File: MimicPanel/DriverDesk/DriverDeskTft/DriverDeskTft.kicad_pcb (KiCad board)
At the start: 4 copper layers, 84.5 x 92 mm, 25 parts, among them SW1 SW_Push, SW10 SW_Push, SW2 SW_Push, SW3 SW_Push, SW4 SW_Push, SW5 SW_Push, SW6 SW_Push, SW7 SW_Push, SW8 SW_Push, SW9 SW_Push

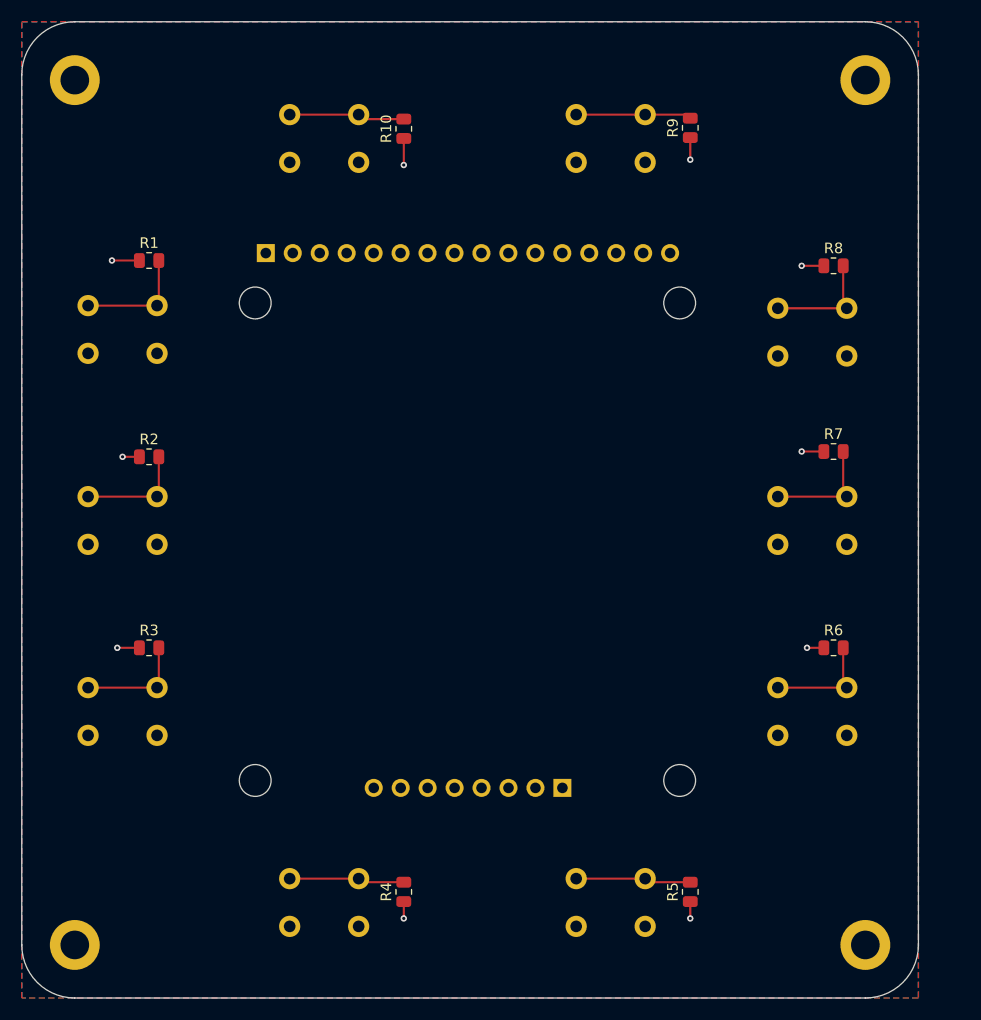
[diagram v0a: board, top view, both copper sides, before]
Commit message: updated positions
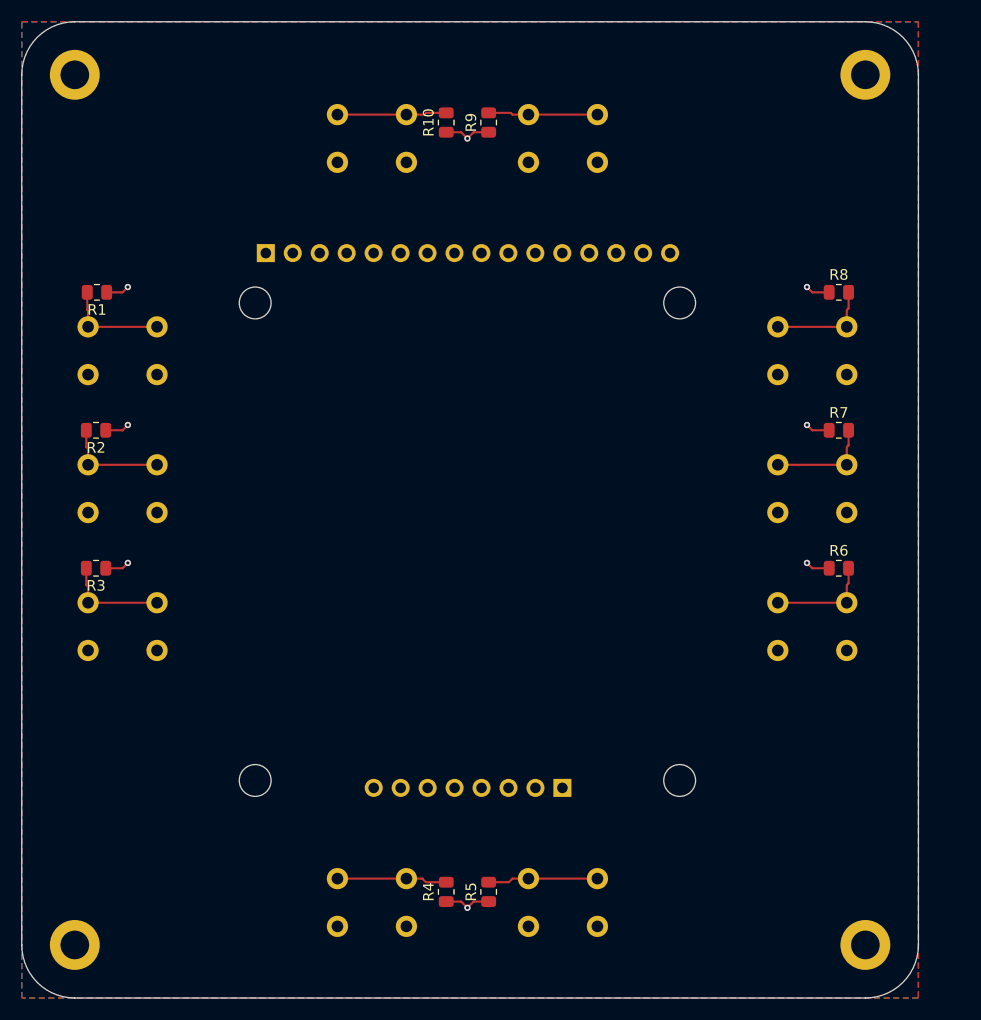
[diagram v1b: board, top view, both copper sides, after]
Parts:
- moved R9 19.0 mm to (102.0, 62.5)
- moved R5 19.0 mm to (102.0, 135.0)
- moved R3 9.01 mm to (65.0, 104.5), turned to 180 degrees
- moved SW3 8.00 mm to (70.8, 107.8)
- moved SW6 8.00 mm to (135.8, 107.8)
- moved R6 7.52 mm to (135.0, 104.5)
- moved R1 5.76 mm to (65.1, 78.5), turned to 180 degrees
- moved R2 5.59 mm to (65.0, 91.5), turned to 180 degrees
- moved SW10 4.50 mm to (94.2, 61.8)
- moved SW4 4.50 mm to (94.2, 133.8)
- moved SW5 4.50 mm to (112.2, 133.8)
- moved SW9 4.50 mm to (112.2, 61.8)
- moved R10 4.04 mm to (98.0, 62.5)
- moved R4 4.00 mm to (98.0, 135.0)
- moved SW2 3.00 mm to (70.8, 94.8)
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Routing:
- net VCC: track 19.8 -> 22.7 mm, vias 10 -> 8
- net /Btn/btn_7: track 10.9 -> 9.82 mm
- net /Btn/btn_1: track 10.8 -> 9.78 mm
- net /Btn/btn_6: track 10.6 -> 9.82 mm
- net /Btn/btn_4: track 10.9 -> 10.3 mm
- net /Btn/btn_8: track 10.4 -> 9.82 mm
- net /Btn/btn_5: track 10.9 -> 10.3 mm
- net /Btn/btn_9: track 10.9 -> 10.4 mm
- net /Btn/btn_3: track 10.3 -> 9.82 mm
- net /Btn/btn_2: track 10.3 -> 9.82 mm
- net /Btn/btn_10: track 10.9 -> 10.4 mm

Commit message: TftModule
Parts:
- SW1, SW10, SW2, SW3, SW4, SW5, SW6, SW7, SW8, SW9: footprint Button_Switch_THT:SW_PUSH_6mm -> Button_Switch_THT:SW_PUSH_6mm_H5mm
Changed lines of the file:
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@@
 		(tags "resistor")
 		(property "Reference" "R2"
-			(at 0 -1.65 360)
+			(at 0 -1.65 0)
 			(layer "F.SilkS")
 			(effects
@@
 		)
 		(property "Value" "R"
-			(at 0 1.65 360)
+			(at 0 1.65 0)
 			(layer "F.Fab")
 			(effects
@@
 		)
 		(fp_text user "${REFERENCE}"
-			(at 0 0 360)
+			(at 0 0 0)
 			(layer "F.Fab")
 			(effects
@@
 		(tags "resistor")
 		(property "Reference" "R3"
-			(at 0 -1.65 360)
+			(at 0 -1.65 0)
 			(layer "F.SilkS")
 			(effects
@@
 		)
 		(property "Value" "R"
-			(at 0 1.65 360)
+			(at 0 1.65 0)
 			(layer "F.Fab")
 			(effects
@@
 		)
 		(fp_text user "${REFERENCE}"
-			(at 0 0 360)
+			(at 0 0 0)
 			(layer "F.Fab")
 			(effects
@@
 		(tags "resistor")
 		(property "Reference" "R1"
-			(at 0 -1.65 360)
+			(at 0 -1.65 0)
 			(layer "F.SilkS")
 			(effects
@@
 		)
 		(property "Value" "R"
-			(at 0 1.65 360)
+			(at 0 1.65 0)
 			(layer "F.Fab")
 			(effects
@@
 		)
 		(fp_text user "${REFERENCE}"
-			(at 0 0 360)
+			(at 0 0 0)
 			(layer "F.Fab")
 			(effects
@@
 		)
 	)
-	(footprint "Button_Switch_THT:SW_PUSH_6mm"
+	(footprint "Button_Switch_THT:SW_PUSH_6mm_H5mm"
 		(layer "B.Cu")
 		(at 94.25 61.75 180)
-		(descr "Generic 6mm SW tactile push button")
+		(descr "tactile push button, 6x6mm e.g. PHAP33xx series, height=5mm")
 		(tags "tact sw push 6mm")
 		(property "Reference" "SW10"
@@
 			)
 		)
-		(property "Footprint" "Button_Switch_THT:SW_PUSH_6mm"
+		(property "Footprint" "Button_Switch_THT:SW_PUSH_6mm_H5mm"
 			(at 0 0 0)
 			(unlocked yes)
@@
 			(pintype "passive")
 		)
-		(model "${KICAD8_3DMODEL_DIR}/Button_Switch_THT.3dshapes/SW_PUSH_6mm.wrl"
+		(model "${KICAD8_3DMODEL_DIR}/Button_Switch_THT.3dshapes/SW_PUSH_6mm_H5mm.wrl"
 			(offset
 				(xyz 0 0 0)
@@
 		)
 	)
-	(footprint "Button_Switch_THT:SW_PUSH_6mm"
+	(footprint "Button_Switch_THT:SW_PUSH_6mm_H5mm"
 		(layer "B.Cu")
 		(at 94.25 133.75 180)
-		(descr "Generic 6mm SW tactile push button")
+		(descr "tactile push button, 6x6mm e.g. PHAP33xx series, height=5mm")
 		(tags "tact sw push 6mm")
 		(property "Reference" "SW4"
@@
 			)
 		)
-		(property "Footprint" "Button_Switch_THT:SW_PUSH_6mm"
+		(property "Footprint" "Button_Switch_THT:SW_PUSH_6mm_H5mm"
 			(at 0 0 0)
 			(unlocked yes)
@@
 			(pintype "passive")
 		)
-		(model "${KICAD8_3DMODEL_DIR}/Button_Switch_THT.3dshapes/SW_PUSH_6mm.wrl"
+		(model "${KICAD8_3DMODEL_DIR}/Button_Switch_THT.3dshapes/SW_PUSH_6mm_H5mm.wrl"
 			(offset
 				(xyz 0 0 0)
@@
 		)
 	)
-	(footprint "Button_Switch_THT:SW_PUSH_6mm"
+	(footprint "Button_Switch_THT:SW_PUSH_6mm_H5mm"
 		(layer "B.Cu")
 		(at 135.75 81.75 180)
-		(descr "Generic 6mm SW tactile push button")
+		(descr "tactile push button, 6x6mm e.g. PHAP33xx series, height=5mm")
 		(tags "tact sw push 6mm")
 		(property "Reference" "SW8"
@@
 			)
 		)
-		(property "Footprint" "Button_Switch_THT:SW_PUSH_6mm"
+		(property "Footprint" "Button_Switch_THT:SW_PUSH_6mm_H5mm"
 			(at 0 0 0)
 			(unlocked yes)
@@
 			(pintype "passive")
 		)
-		(model "${KICAD8_3DMODEL_DIR}/Button_Switch_THT.3dshapes/SW_PUSH_6mm.wrl"
+		(model "${KICAD8_3DMODEL_DIR}/Button_Switch_THT.3dshapes/SW_PUSH_6mm_H5mm.wrl"
 			(offset
 				(xyz 0 0 0)
@@
 		)
 	)
-	(footprint "Button_Switch_THT:SW_PUSH_6mm"
+	(footprint "Button_Switch_THT:SW_PUSH_6mm_H5mm"
 		(layer "B.Cu")
 		(at 70.75 94.75 180)
-		(descr "Generic 6mm SW tactile push button")
+		(descr "tactile push button, 6x6mm e.g. PHAP33xx series, height=5mm")
 		(tags "tact sw push 6mm")
 		(property "Reference" "SW2"
@@
 			)
 		)
-		(property "Footprint" "Button_Switch_THT:SW_PUSH_6mm"
+		(property "Footprint" "Button_Switch_THT:SW_PUSH_6mm_H5mm"
 			(at 0 0 0)
 			(unlocked yes)
@@
 			(pintype "passive")
 		)
-		(model "${KICAD8_3DMODEL_DIR}/Button_Switch_THT.3dshapes/SW_PUSH_6mm.wrl"
+		(model "${KICAD8_3DMODEL_DIR}/Button_Switch_THT.3dshapes/SW_PUSH_6mm_H5mm.wrl"
 			(offset
 				(xyz 0 0 0)
@@
 		)
 	)
-	(footprint "Button_Switch_THT:SW_PUSH_6mm"
+	(footprint "Button_Switch_THT:SW_PUSH_6mm_H5mm"
 		(layer "B.Cu")
 		(at 112.25 133.75 180)
-		(descr "Generic 6mm SW tactile push button")
+		(descr "tactile push button, 6x6mm e.g. PHAP33xx series, height=5mm")
 		(tags "tact sw push 6mm")
 		(property "Reference" "SW5"
@@
 			)
 		)
-		(property "Footprint" "Button_Switch_THT:SW_PUSH_6mm"
+		(property "Footprint" "Button_Switch_THT:SW_PUSH_6mm_H5mm"
 			(at 0 0 0)
 			(unlocked yes)
@@
 			(pintype "passive")
 		)
-		(model "${KICAD8_3DMODEL_DIR}/Button_Switch_THT.3dshapes/SW_PUSH_6mm.wrl"
+		(model "${KICAD8_3DMODEL_DIR}/Button_Switch_THT.3dshapes/SW_PUSH_6mm_H5mm.wrl"
 			(offset
 				(xyz 0 0 0)
@@
 		)
 	)
-	(footprint "Button_Switch_THT:SW_PUSH_6mm"
+	(footprint "Button_Switch_THT:SW_PUSH_6mm_H5mm"
 		(layer "B.Cu")
 		(at 135.75 94.75 180)
-		(descr "Generic 6mm SW tactile push button")
+		(descr "tactile push button, 6x6mm e.g. PHAP33xx series, height=5mm")
 		(tags "tact sw push 6mm")
 		(property "Reference" "SW7"
@@
 			)
 		)
-		(property "Footprint" "Button_Switch_THT:SW_PUSH_6mm"
+		(property "Footprint" "Button_Switch_THT:SW_PUSH_6mm_H5mm"
 			(at 0 0 0)
 			(unlocked yes)
@@
 			(pintype "passive")
 		)
-		(model "${KICAD8_3DMODEL_DIR}/Button_Switch_THT.3dshapes/SW_PUSH_6mm.wrl"
+		(model "${KICAD8_3DMODEL_DIR}/Button_Switch_THT.3dshapes/SW_PUSH_6mm_H5mm.wrl"
 			(offset
 				(xyz 0 0 0)
@@
 		)
 	)
-	(footprint "Button_Switch_THT:SW_PUSH_6mm"
+	(footprint "Button_Switch_THT:SW_PUSH_6mm_H5mm"
 		(layer "B.Cu")
 		(at 70.75 81.75 180)
-		(descr "Generic 6mm SW tactile push button")
+		(descr "tactile push button, 6x6mm e.g. PHAP33xx series, height=5mm")
 		(tags "tact sw push 6mm")
 		(property "Reference" "SW1"
@@
 			)
 		)
-		(property "Footprint" "Button_Switch_THT:SW_PUSH_6mm"
+		(property "Footprint" "Button_Switch_THT:SW_PUSH_6mm_H5mm"
 			(at 0 0 0)
 			(unlocked yes)
@@
 			(pintype "passive")
 		)
-		(model "${KICAD8_3DMODEL_DIR}/Button_Switch_THT.3dshapes/SW_PUSH_6mm.wrl"
+		(model "${KICAD8_3DMODEL_DIR}/Button_Switch_THT.3dshapes/SW_PUSH_6mm_H5mm.wrl"
 			(offset
 				(xyz 0 0 0)
@@
 		)
 	)
-	(footprint "Button_Switch_THT:SW_PUSH_6mm"
+	(footprint "Button_Switch_THT:SW_PUSH_6mm_H5mm"
 		(layer "B.Cu")
 		(at 70.75 107.75 180)
-		(descr "Generic 6mm SW tactile push button")
+		(descr "tactile push button, 6x6mm e.g. PHAP33xx series, height=5mm")
 		(tags "tact sw push 6mm")
 		(property "Reference" "SW3"
@@
 			)
 		)
-		(property "Footprint" "Button_Switch_THT:SW_PUSH_6mm"
+		(property "Footprint" "Button_Switch_THT:SW_PUSH_6mm_H5mm"
 			(at 0 0 0)
 			(unlocked yes)
@@
 			(pintype "passive")
 		)
-		(model "${KICAD8_3DMODEL_DIR}/Button_Switch_THT.3dshapes/SW_PUSH_6mm.wrl"
+		(model "${KICAD8_3DMODEL_DIR}/Button_Switch_THT.3dshapes/SW_PUSH_6mm_H5mm.wrl"
 			(offset
 				(xyz 0 0 0)
@@
 		)
 	)
-	(footprint "Button_Switch_THT:SW_PUSH_6mm"
+	(footprint "Button_Switch_THT:SW_PUSH_6mm_H5mm"
 		(layer "B.Cu")
 		(at 135.75 107.75 180)
-		(descr "Generic 6mm SW tactile push button")
+		(descr "tactile push button, 6x6mm e.g. PHAP33xx series, height=5mm")
 		(tags "tact sw push 6mm")
 		(property "Reference" "SW6"
@@
 			)
 		)
-		(property "Footprint" "Button_Switch_THT:SW_PUSH_6mm"
+		(property "Footprint" "Button_Switch_THT:SW_PUSH_6mm_H5mm"
 			(at 0 0 0)
 			(unlocked yes)
@@
 			(pintype "passive")
 		)
-		(model "${KICAD8_3DMODEL_DIR}/Button_Switch_THT.3dshapes/SW_PUSH_6mm.wrl"
+		(model "${KICAD8_3DMODEL_DIR}/Button_Switch_THT.3dshapes/SW_PUSH_6mm_H5mm.wrl"
 			(offset
 				(xyz 0 0 0)
@@
 		)
 	)
-	(footprint "Button_Switch_THT:SW_PUSH_6mm"
+	(footprint "Button_Switch_THT:SW_PUSH_6mm_H5mm"
 		(layer "B.Cu")
 		(at 112.25 61.75 180)
-		(descr "Generic 6mm SW tactile push button")
+		(descr "tactile push button, 6x6mm e.g. PHAP33xx series, height=5mm")
 		(tags "tact sw push 6mm")
 		(property "Reference" "SW9"
@@
 			)
 		)
-		(property "Footprint" "Button_Switch_THT:SW_PUSH_6mm"
+		(property "Footprint" "Button_Switch_THT:SW_PUSH_6mm_H5mm"
 			(at 0 0 0)
 			(unlocked yes)
@@
 			(pintype "passive")
 		)
-		(model "${KICAD8_3DMODEL_DIR}/Button_Switch_THT.3dshapes/SW_PUSH_6mm.wrl"
+		(model "${KICAD8_3DMODEL_DIR}/Button_Switch_THT.3dshapes/SW_PUSH_6mm_H5mm.wrl"
 			(offset
 				(xyz 0 0 0)

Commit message: rot enc
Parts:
- added R11: R, Resistor_SMD:R_1206_3216Metric, F.Cu at (144.3, 118.7)
- added R12: R, Resistor_SMD:R_1206_3216Metric, F.Cu at (144.3, 122.0)
- added R13: R, Resistor_SMD:R_1206_3216Metric, F.Cu at (144.3, 125.3)
- added R14: R, Resistor_SMD:R_1206_3216Metric, F.Cu at (144.3, 128.6)
- added SW11: RotaryEncoder_Switch, Rotary_Encoder:RotaryEncoder_Alps_EC11E-Switch_Vertical_H20mm, B.Cu at (139.4, 124.6)
- added SW12: SW_Push, Button_Switch_THT:SW_PUSH_6mm_H5mm, B.Cu at (80.2, 122.2)
- R1, R10, R2, R3, R4, R5, R6, R7, R8, R9: footprint Resistor_SMD:R_0805_2012Metric -> Resistor_SMD:R_1206_3216Metric

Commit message: Update btns
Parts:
- SW11: footprint Rotary_Encoder:RotaryEncoder_Alps_EC11E-Switch_Vertical_H20mm -> DigitalTrains:XDCR_PEC11R-4215F-S0024
- moved R13 74.3 mm to (71.2, 138.4), turned to 90 degrees
- moved SW11 71.9 mm to (67.5, 126.8)
- moved R12 71.4 mm to (74.8, 138.4), turned to 90 degrees
- moved R14 67.5 mm to (77.4, 120.2), turned to 90 degrees
- moved SW12 55.4 mm to (135.5, 124.5)
- moved R11 10.2 mm to (134.5, 121.2)
- moved R1 0.26 mm to (65.0, 78.2)
- moved R2 0.25 mm to (65.0, 91.2)
- moved R3 0.25 mm to (65.0, 104.2)
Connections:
- SW11 pad MP: (no net) -> GND
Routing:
- net /Btn/btn_H: track 0.00 -> 9.94 mm
- net /Btn/btn_RB: track 0.00 -> 8.57 mm
- net /Btn/btn_RS: track 0.00 -> 7.82 mm
- net /Btn/btn_RA: track 0.00 -> 7.15 mm
- net VCC: track 22.7 -> 28.9 mm, vias 8 -> 11
- net /Btn/btn_1: track 9.78 -> 10.3 mm

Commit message: headers
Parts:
- added J1: Conn_01x06, Connector_PinHeader_2.54mm:PinHeader_1x08_P2.54mm_Vertical, F.Cu at (91.2, 121.1)
- added J2: Conn_01x04, Connector_PinHeader_2.54mm:PinHeader_1x04_P2.54mm_Vertical, F.Cu at (81.0, 131.5)
- added J3: Conn_02x05_Odd_Even, Connector_PinHeader_2.54mm:PinHeader_2x05_P2.54mm_Vertical, F.Cu at (127.0, 60.2)
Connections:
- net /Btn/btn_1 renamed /Btn1
- net /Btn/btn_10 renamed /Btn10
- net /Btn/btn_2 renamed /Btn2
- net /Btn/btn_3 renamed /Btn3
- net /Btn/btn_4 renamed /Btn4
- net /Btn/btn_5 renamed /Btn5
- net /Btn/btn_6 renamed /Btn6
- net /Btn/btn_7 renamed /Btn7
- net /Btn/btn_8 renamed /Btn8
- net /Btn/btn_9 renamed /Btn9
- net /Btn/btn_H renamed /BtnH
- net /Btn/btn_RA renamed /RA
- net /Btn/btn_RB renamed /RB
- net /Btn/btn_RS renamed /RS
- U1 pad 18: unconnected-(U1-BL-Pad18) -> /BL
- U1 pad 20: unconnected-(U1-CLK-Pad20) -> /CLK
- U1 pad 21: unconnected-(U1-DIN-Pad21) -> /DIN
- U1 pad 22: unconnected-(U1-D/C-Pad22) -> /DC
- U1 pad 23: unconnected-(U1-CS-Pad23) -> /CS
- U1 pad 24: unconnected-(U1-RST-Pad24) -> /RST
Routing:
- net /Btn10: track 10.4 -> 118.6 mm, vias 0 -> 1
- net /Btn3: track 10.3 -> 101.8 mm
- net /Btn9: track 10.4 -> 99.2 mm
- net /Btn2: track 10.3 -> 90.2 mm
- net /Btn1: track 10.3 -> 78.6 mm
- net /BtnH: track 9.94 -> 60.8 mm
- net /Btn8: track 9.82 -> 55.3 mm
- net /Btn4: track 10.3 -> 47.8 mm
- net /RS: track 7.82 -> 36.6 mm
- net /Btn7: track 9.82 -> 38.3 mm
- net /Btn5: track 10.3 -> 28.6 mm
- net /Btn6: track 9.82 -> 21.8 mm
- net /RB: track 8.57 -> 19.8 mm
- net /RA: track 7.15 -> 14.0 mm
- net /CS: track 0.00 -> 4.12 mm
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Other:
- board text added: "1 2 3 4 5"
- board text added: "10 9 8 7 6"
- board text added: "H A B S"
- board text added: "RST CS DC DIN CLK VCC BL GND"

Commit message: Gnd Pour
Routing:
- added copper zone on In2.Cu, net GND
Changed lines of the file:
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@@
 		(net 2)
 		(net_name "GND")
-		(layers "F&B.Cu")
+		(layers "F.Cu" "In2.Cu" "B.Cu")
 		(hatch edge 0.5)
 		(connect_pads
